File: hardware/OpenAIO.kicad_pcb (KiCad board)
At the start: 8 copper layers, 35 x 35 mm, 285 parts, among them J1 OpenDrone-Core, J10 5V, J12 5V, J13 5V, J14 5V, J15 5V, J16 5V, J17 5V, J18 5V, J19 5V, J2 Conn_Coaxial_Small, J20 5V, J21 5V, J22 5V, J23 5V, J24 5V, J25 5V, J26 5V, J27 5V, J28 5V, J29 5V, J3 5V, J30 5V, J31 5V, J32 5V, J35 5V, J36 5V, J37 5V, J38 5V, J4 5V, J5 5V, J6 5V, J8 5V, J9 5V, Q1 DOY180N03T, Q10 DOY180N03T, Q11 DOY180N03T, Q12 DOY180N03T, Q13 DOY180N03T, Q14 DOY180N03T, Q15 DOY180N03T, Q16 DOY180N03T, Q17 DOY180N03T, Q18 DOY180N03T, Q19 DOY180N03T, Q2 DOY180N03T, Q20 DOY180N03T, Q21 DOY180N03T, Q22 DOY180N03T, Q23 DOY180N03T, Q24 DOY180N03T, Q3 DOY180N03T, Q4 DOY180N03T, Q5 DOY180N03T, Q6 DOY180N03T, Q7 DOY180N03T, Q8 DOY180N03T, Q9 DOY180N03T, T1 0900PC16J0042001E, U1 AIO_outline, U10 SM06B-SRSS-TB(LF)(SN), U11 AT32F421G8U7, U12 NSG2065Q, U13 AT32F421G8U7, U14 NSG2065Q, U15 AT32F421G8U7, U16 NSG2065Q, U17 AT32F421G8U7, U18 NSG2065Q, U19 INA186A3IDCKR, U22 TS2306A 240GF MSM 9_C2976675, U3 LR1121IMLTRT, U4 ESP32-C3, U5 RFX2401C, U6 TLV75533PDQNR, U7 SKY13373-460LF, U8 LMR51430YFDDCR, U9 LMR51430YFDDCR, X1 CJ17-400001010B20

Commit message: feat(hardware): 8-layer HDI 1+6+1 routing setup (NextPCB)
Layer types (In1, In6 power; In2-In5 mixed), constraints, pre-defined track
and via sizes, net classes, layer pair presets, HDI via rules in the
.kicad_dru, routing how-to and stackup legend on Cmts.User, AGENTS.md and
README.md stackup statements. Removes the two 2 oz outer copper rules.
No track, via, zone or footprint changed. The physical stackup is not set
(no API writes it).

Co-Authored-By: Claude Opus 5.5 <noreply@anthropic.com>
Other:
- board text added: "HDI 1+6+1 NextPCB. L1 parts | L2 GND | L3 sig | L4 PWR | L5 PWR | L6 sig | L7 GND | L8 parts Vias: laser 0.25/0.10 L1-L2, L8-L7 | buried L2-L7 and through 0.40/0.20 default (power 0.45/0.25) | legacy through 0.35/0.20 Route (X). V = through via. Ctrl+V = microvia. Alt+Shift+V = blind/buried via (uses active layer pair). Layer pair presets are preloaded (Route > Set Layer Pair): "Buried L2-L7" In1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"
- board text added: "OpenAIO STACKUP 1.6 mm, 8 layer HDI 1+6+1, all copper 1 oz (0.035), mask 0.015 Layer | KiCad | Use | Dielectric below (mm) L1 | F.Cu | parts, RF, USB, power loops | 1080 0.077 L2 | In1.Cu | GND plane, no tracks (type power) | 2116 0.125 L3 | In2.Cu | signals + +BATT zone (mixed) | core 0.330 L4 | In3.Cu | +4v5/+3V3/+5V_USB zones + signals | 2116+2313 0.228 L5 | In4.Cu | +5V/+3V3 zones + signals |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"
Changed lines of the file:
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@@
 	(layers
 		(0 "F.Cu" signal)
-		(4 "In1.Cu" signal)
-		(6 "In2.Cu" signal)
-		(8 "In3.Cu" signal)
-		(10 "In4.Cu" signal)
-		(12 "In5.Cu" signal)
-		(14 "In6.Cu" signal)
+		(4 "In1.Cu" power)
+		(6 "In2.Cu" mixed)
+		(8 "In3.Cu" mixed)
+		(10 "In4.Cu" mixed)
+		(12 "In5.Cu" mixed)
+		(14 "In6.Cu" power)
 		(2 "B.Cu" signal)
 		(9 "F.Adhes" user "F.Adhesive")
@@
 		)
 	)
+	(gr_text "HDI 1+6+1 NextPCB. L1 parts | L2 GND | L3 sig | L4 PWR | L5 PWR | L6 sig | L7 GND | L8 parts\nVias: laser 0.25/0.10 L1-L2, L8-L7 | buried L2-L7 and through 0.40/0.20 default (power 0.45/0.25) | legacy through 0.35/0.20\nRoute (X). V = through via. Ctrl+V = microvia. Alt+Shift+V = blind/buried via (uses active layer pair).\nLayer pair presets are preloaded (Route > Set Layer Pair): \"Buried L2-L7\" In1.Cu/In6.Cu, \"Outer F-B\"; Shift+V cycles.\nAlt+< = select layer then place blind/buried via. After placing, E on the via: check type and layers.\nSizes: Board Setup > Design Rules > Pre-defined Sizes; pick via size in the toolbar before placing.\nGND pin: pad > Ctrl+V microvia into the pad > done (L2 is GND). Bottom: pad > Ctrl+V to In6.\nSignal: pad > Ctrl+V to In1 > Alt+Shift+V buried 0.25 mm beside it (lands overlap, no L2 track) > route on In2/In5.\nPower: pad > microvias > buried vias staggered > In3/In4 plane connects through the buried via.\nNever stack a microvia on a buried via; stagger 0.25 mm c-c. Never microvia L1-L3 (skip via).\nFine pitch (<= 0.5 mm): microvia in pad, filled and capped (IPC-4761 VII). Buried vias are resin filled.\nPower and phase: arrays of microvias and buried vias, 0.20 mm same-net hole spacing.\nRF: no vias on RF nets, 0.105 mm CPWG gap 0.15 on L1/L8, L2/L7 solid below.\nRun DRC after each block; \"blind via\" errors mean Alt+Shift+V picked the wrong type."
+		(at 96 43.5 0)
+		(layer "Cmts.User")
+		(effects
+			(font
+				(size 1 1)
+				(line_spacing 1.4)
+				(thickness 0.15)
+			)
+			(justify left top)
+		)
+	)
+	(gr_text "OpenAIO STACKUP 1.6 mm, 8 layer HDI 1+6+1, all copper 1 oz (0.035), mask 0.015\nLayer | KiCad | Use                                   | Dielectric below (mm)\nL1 | F.Cu   | parts, RF, USB, power loops             | 1080 0.077\nL2 | In1.Cu | GND plane, no tracks (type power)       | 2116 0.125\nL3 | In2.Cu | signals + +BATT zone (mixed)           | core 0.330\nL4 | In3.Cu | +4v5/+3V3/+5V_USB zones + signals       | 2116+2313 0.228\nL5 | In4.Cu | +5V/+3V3 zones + signals                | core 0.330\nL6 | In5.Cu | signals + +10V/+BATT zones              | 2116 0.125\nL7 | In6.Cu | GND plane, no tracks (type power)       | 1080 0.077\nL8 | B.Cu   | parts, RF, power\nVIA | span | drill/pad (mm)\nLaser micro | F.Cu-In1.Cu, In6.Cu-B.Cu | 0.10/0.25\nBuried | In1.Cu-In6.Cu | 0.20/0.40 (power 0.25/0.45)\nThrough | F.Cu-B.Cu | 0.20/0.35 legacy, 0.20/0.40 default, 0.25/0.45, 0.30/0.50\nBlind mechanical: not allowed (DRC rule)"
+		(at 96 73 0)
+		(layer "Cmts.User")
+		(effects
+			(font
+				(size 1 1)
+				(line_spacing 1.4)
+				(thickness 0.15)
+			)
+			(justify left top)
+		)
+	)

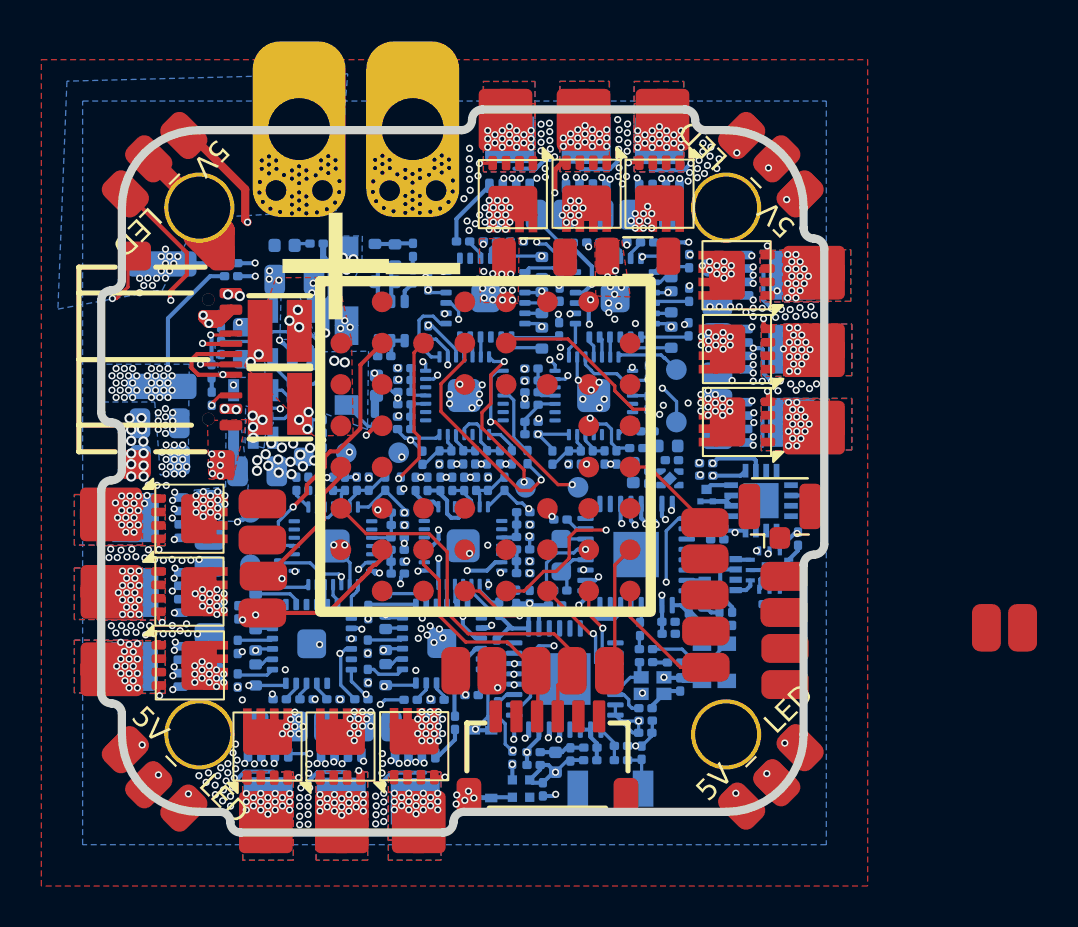
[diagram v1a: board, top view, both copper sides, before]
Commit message: Remove all tracks and vias for the full 8L HDI re-route
Placement, zones and rule areas are kept: 285 footprints, 48 zones.
Removed 1775 track segments and 1091 vias with the pcbnew API.

Co-Authored-By: Claude Opus 5.5 <noreply@anthropic.com>
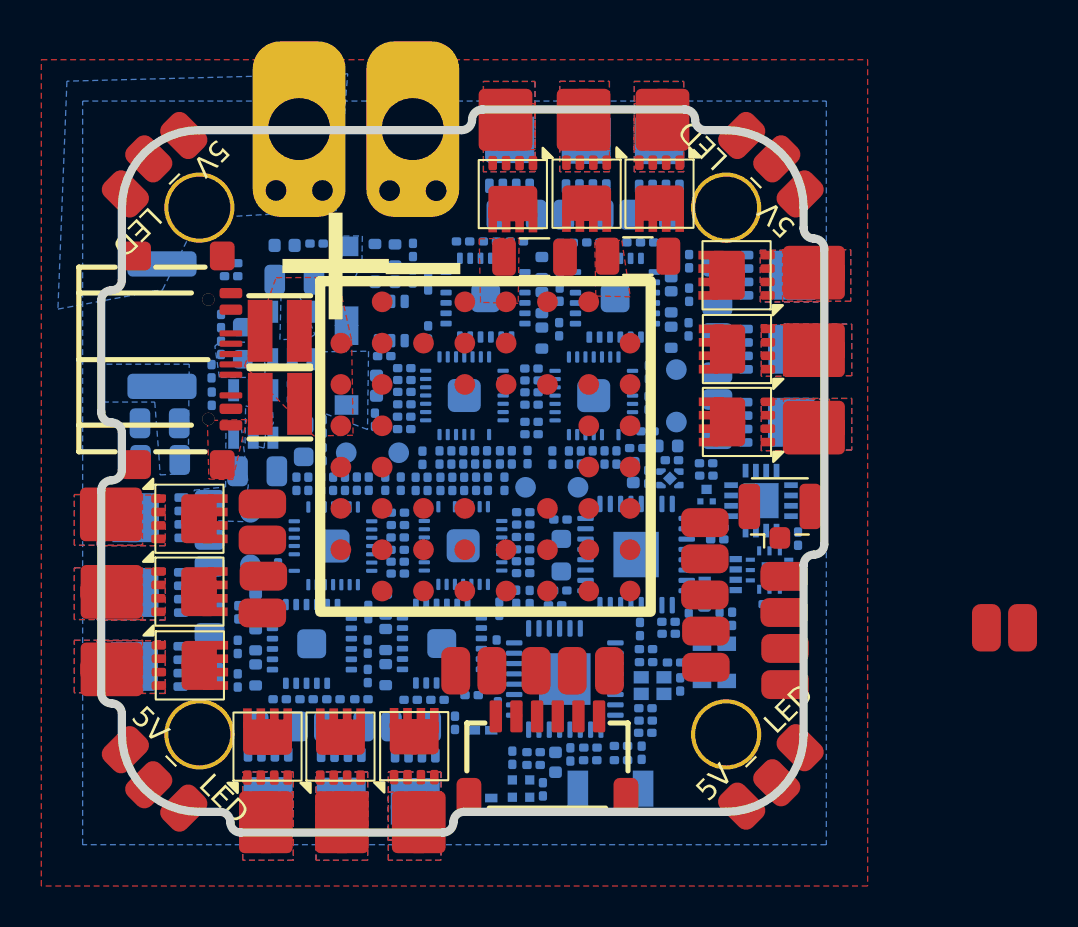
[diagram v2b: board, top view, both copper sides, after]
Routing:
- net /LED: track 109.9 -> 0.00 mm, vias 6 -> 0
- net GND: track 92.3 -> 0.00 mm, vias 373 -> 0
- net +3V3: track 48.5 -> 0.00 mm, vias 15 -> 0
- net /1C: track 23.3 -> 0.00 mm, vias 20 -> 0
- net /1A: track 23.1 -> 0.00 mm, vias 21 -> 0
- net /4C: track 22.3 -> 0.00 mm, vias 20 -> 0
- net /3A: track 21.3 -> 0.00 mm, vias 21 -> 0
- net /2A: track 20.9 -> 0.00 mm, vias 21 -> 0
- net /2B: track 20.7 -> 0.00 mm, vias 21 -> 0
- net /3B: track 19.6 -> 0.00 mm, vias 20 -> 0
- net /1B: track 19.3 -> 0.00 mm, vias 21 -> 0
- net /Pads/UART0_RX: track 19.2 -> 0.00 mm
- net /3C: track 19.0 -> 0.00 mm, vias 21 -> 0
- net /4B: track 18.0 -> 0.00 mm, vias 20 -> 0
- net /2C: track 18.0 -> 0.00 mm, vias 21 -> 0
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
